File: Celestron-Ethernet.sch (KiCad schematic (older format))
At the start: 60 parts, among them J1 FTDI, J2 RJ45_Amphenol_RJMG1BD3B8K1ANR, J3 6P6C, SW1 SW_Push, SW2 SW_DIP_x02, U1 W5500, U2 ATmega328P-AU, U3 74AHC1G125, U4 NCV33375ST-3.3, Y1 8MHz, Y2 25MHz

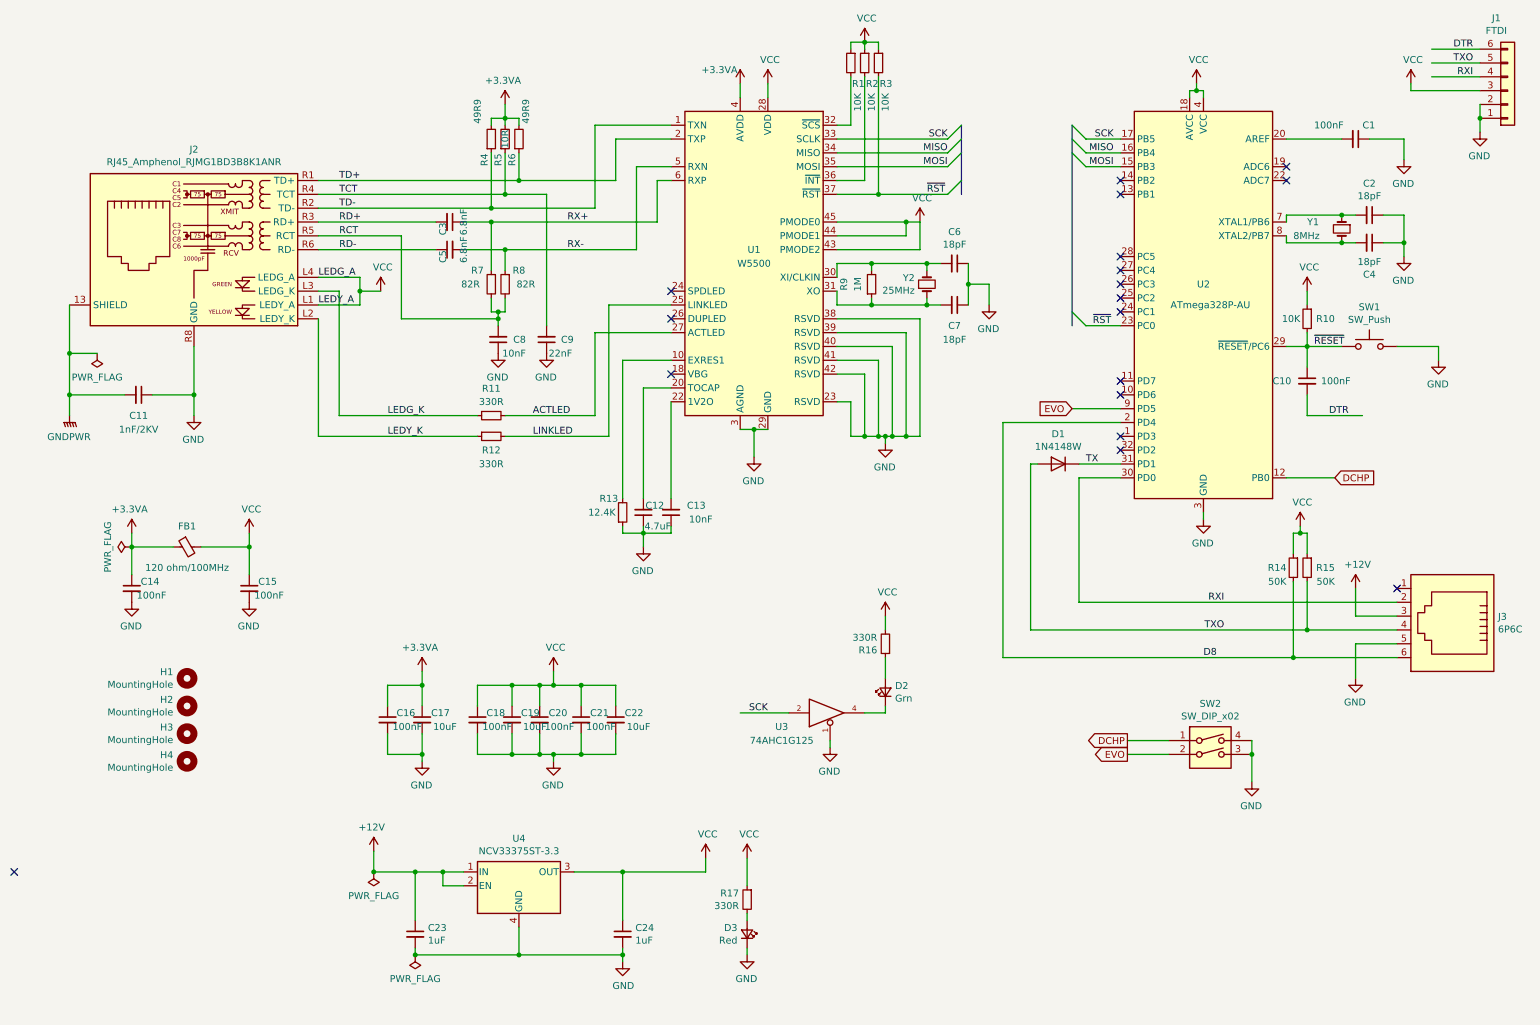
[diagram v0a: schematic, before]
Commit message: Added GPS connectors
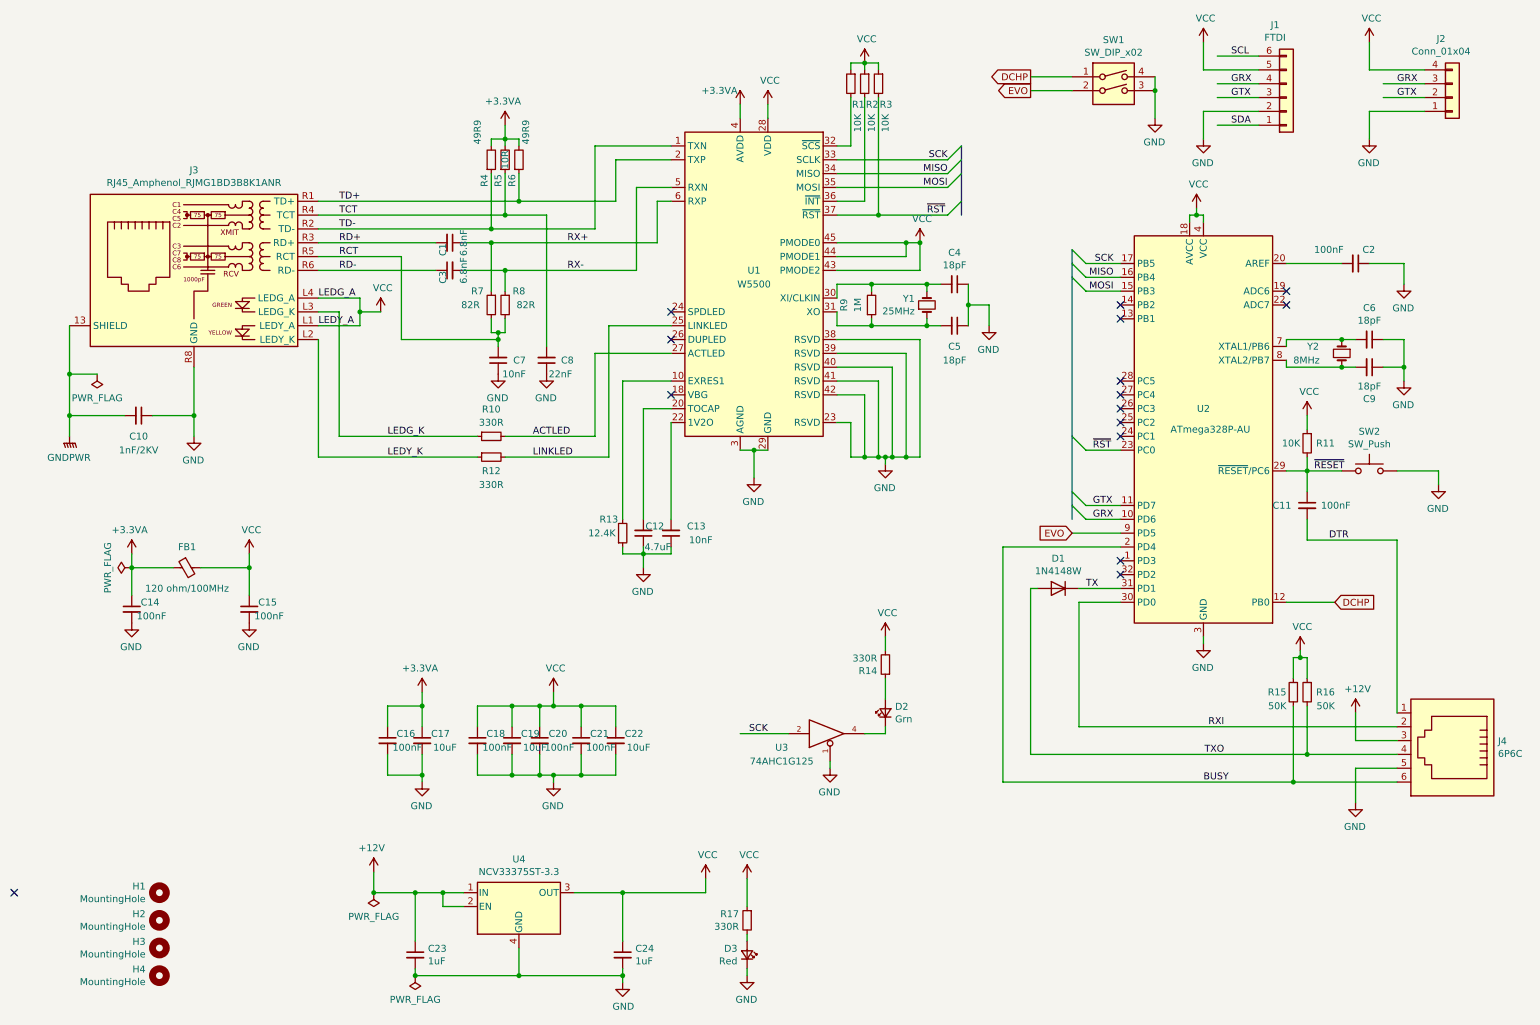
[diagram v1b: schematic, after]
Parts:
- added J2: Conn_01x04, Connector_JST:JST_SH_SM04B-SRSS-TB_1x04-1MP_P1.00mm_Horizontal, symbol Connector_Generic:Conn_01x04
- J1: footprint Connector_PinHeader_2.54mm:PinHeader_1x06_P2.54mm_Horizontal -> Connector_JST:JST_GH_SM06B-GHS-TB_1x06-1MP_P1.25mm_Horizontal
- renumbered C3 to C1, C11 to C10, C10 to C11, C1 to C2, C5 to C3, C6 to C4, C7 to C5, C2 to C6, C8 to C7, C9 to C8, C4 to C9, J2 to J3, J3 to J4, R11 to R10, R10 to R11, R16 to R14, R14 to R15, R15 to R16, SW2 to SW1, SW1 to SW2, Y2 to Y1, Y1 to Y2
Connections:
- net DTR: now also J4.1; no longer J1.6 (Pin_6)
- net GND: now also J2.1 (Pin_1); no longer J1.1 (Pin_1)
- net RXI: no longer J1.4 (Pin_4)
- net TXO: no longer J1.5 (Pin_5)
- net VCC: now also J1.5 (Pin_5), J2.4 (Pin_4); no longer J1.3 (Pin_3)
- net GRX: now reaches U2.10 (PD6)
- net GRX: now also J1.4 (Pin_4), J2.3 (Pin_3)
- net GTX: now reaches U2.11 (PD7)
- net GTX: now also J1.3 (Pin_3), J2.2 (Pin_2)
- net D8 renamed BUSY
- new net SCL: J1.6 (Pin_6)
- new net SDA: J1.1 (Pin_1)
- no-connect marks 18 -> 15
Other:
- moved on the sheet: C1, C10, C11, C12, C13, C14, C15, C16, C17, C18, C19, C2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

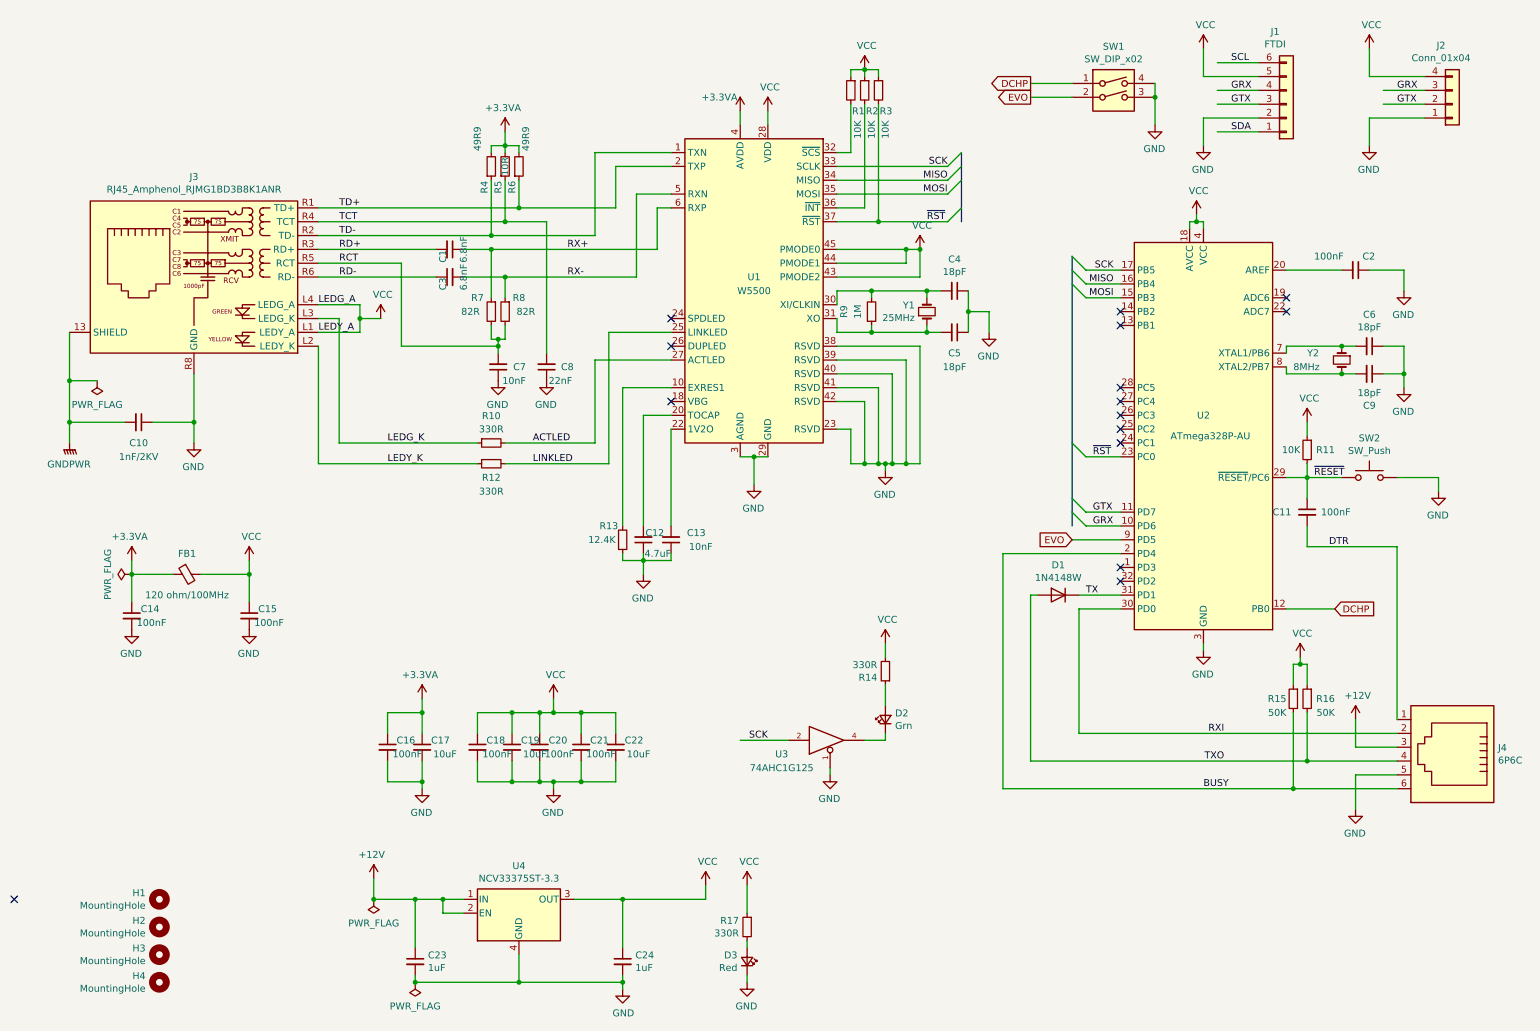
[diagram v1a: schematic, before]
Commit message: Separated W5500 schematic, added joystick interface
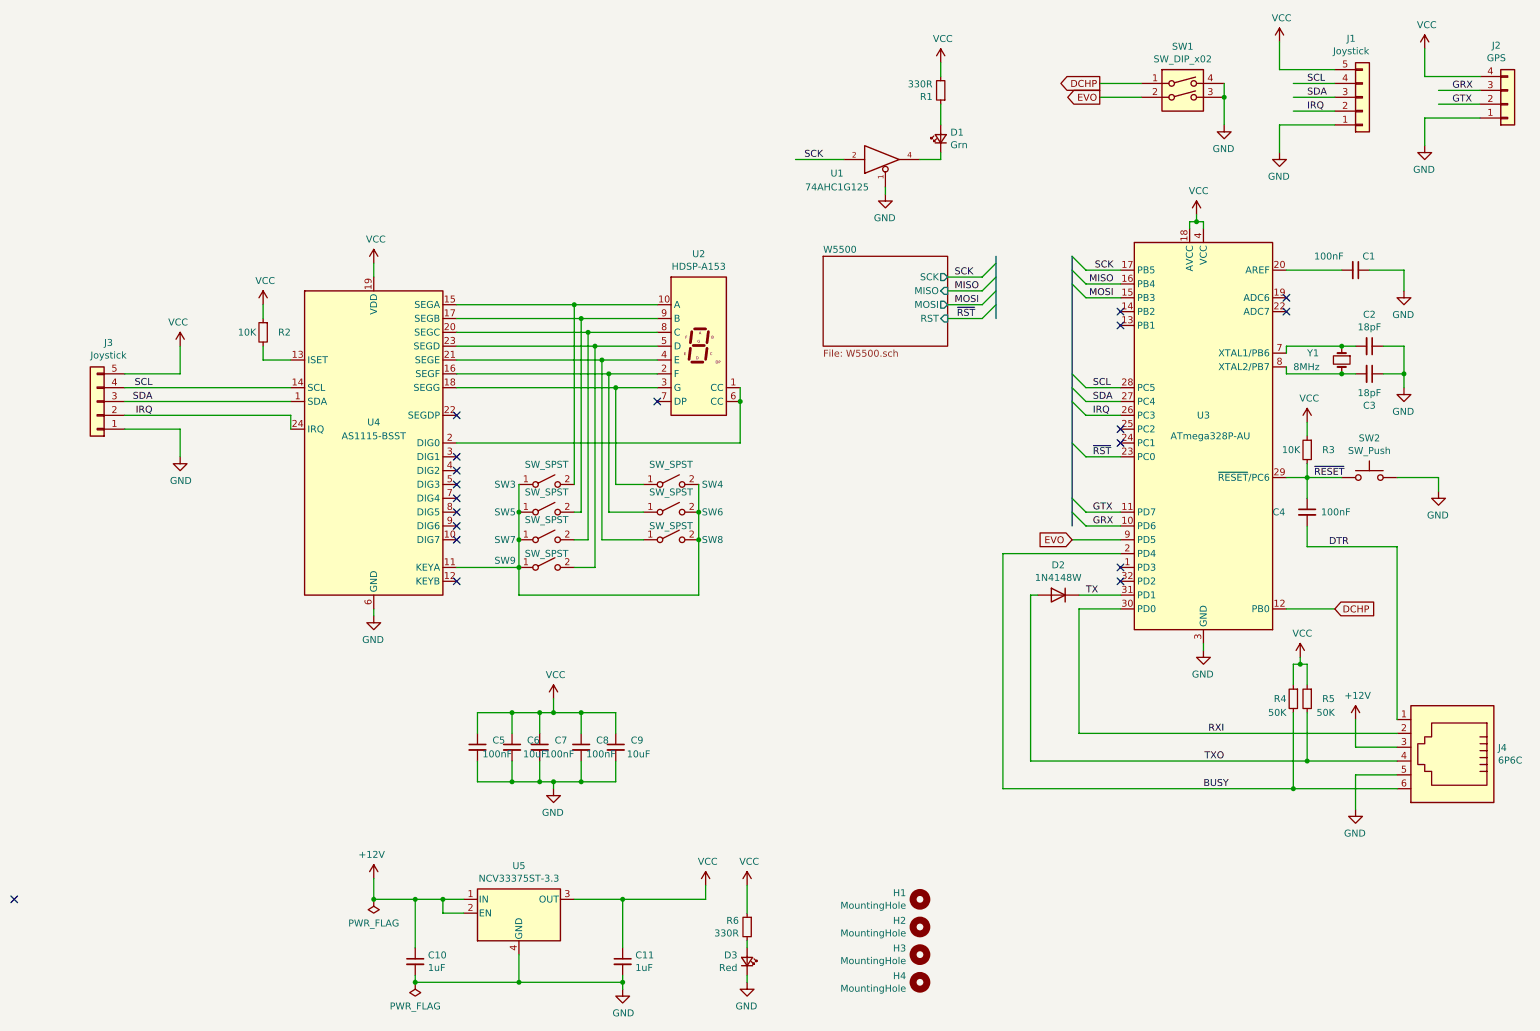
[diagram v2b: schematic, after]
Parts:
- removed C1, C3: 6.8nF, Capacitor_SMD:C_0603_1608Metric, symbol Device:C_Small
- removed C10: 1nF/2KV, Capacitor_SMD:C_1206_3216Metric, symbol Device:C_Small
- removed C12: 4.7uF, Capacitor_SMD:C_0603_1608Metric, symbol Device:C_Small
- removed C13, C7: 10nF, Capacitor_SMD:C_0603_1608Metric, symbol Device:C_Small
- removed C14, C15, C16: 100nF, Capacitor_SMD:C_0603_1608Metric, symbol Device:C_Small
- removed C17: 10uF, Capacitor_SMD:C_0603_1608Metric, symbol Device:C_Small
- removed C4, C5: 18pF, Capacitor_SMD:C_0603_1608Metric, symbol Device:C_Small
- removed C8: 22nF, Capacitor_SMD:C_0603_1608Metric, symbol Device:C_Small
- removed FB1: 120 ohm/100MHz, Inductor_SMD:L_0603_1608Metric, symbol Device:Ferrite_Bead_Small
- removed J1: FTDI, Connector_JST:JST_GH_SM06B-GHS-TB_1x06-1MP_P1.25mm_Horizontal, symbol Connector_Generic:Conn_01x06
- removed J3: RJ45_Amphenol_RJMG1BD3B8K1ANR, Connector_RJ:RJ45_Amphenol_RJMG1BD3B8K1ANR, symbol Connector:RJ45_Amphenol_RJMG1BD3B8K1ANR
- removed R1, R3: 10K, Resistor_SMD:R_0603_1608Metric, symbol Device:R_Small
- removed R10, R12: 330R, Resistor_SMD:R_0603_1608Metric, symbol Device:R_Small
- removed R13: 12.4K, Resistor_SMD:R_0603_1608Metric, symbol Device:R_Small
- removed R4, R6: 49R9, Resistor_SMD:R_0603_1608Metric, symbol Device:R_Small
- removed R5: 10R, Resistor_SMD:R_0603_1608Metric, symbol Device:R_Small
- removed R7, R8: 82R, Resistor_SMD:R_0603_1608Metric, symbol Device:R_Small
- removed R9: 1M, Resistor_SMD:R_0603_1608Metric, symbol Device:R_Small
- removed U1: W5500, Package_QFP:LQFP-48_7x7mm_P0.5mm, symbol Interface_Ethernet:W5500
- removed Y1: 25MHz, Crystal:Crystal_SMD_0603-2Pin_6.0x3.5mm, symbol Device:Crystal_Small
- added J1, J3: Joystick, Connector_JST:JST_SH_SM04B-SRSS-TB_1x05-1MP_P1.00mm_Horizontal, symbol Connector_Generic:Conn_01x05
- added SW3, SW4, SW5, SW6, SW7, SW8, SW9: SW_SPST, symbol Switch:SW_SPST
- added U2: HDSP-A153, Display_7Segment:HDSP-A151, symbol Display_Character:HDSP-A153
- added U4: AS1115-BSST, Package_SO:QSOP-24_3.9x8.7mm_P0.635mm, symbol Interface_Expansion:AS1115-BSST
- J2: value Conn_01x04 -> GPS
- renumbered C2 to C1, C23 to C10, C24 to C11, C6 to C2, C9 to C3, C11 to C4, C18 to C5, C19 to C6, C20 to C7, C21 to C8, C22 to C9, D2 to D1, D1 to D2, R14 to R1, R11 to R3, R15 to R4, R16 to R5, R17 to R6, U3 to U1, U2 to U3, U4 to U5, Y2 to Y1
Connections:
- net labels added: IRQ
- net labels removed: +3.3VA, ACTLED, GNDPWR, LEDG_A, LEDG_K, LEDY_A, LEDY_K, LINKLED, RCT, RD+, RD-, RX+, RX-, TCT, TD+, TD-
- wire segments 277 -> 184
- no-connect marks 15 -> 19
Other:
- moved on the sheet: D1, H1, H2, H3, H4, J2, R1, SW1, U1

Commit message: joystick interface
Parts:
- removed J3: Joystick, Connector_JST:JST_SH_SM04B-SRSS-TB_1x05-1MP_P1.00mm_Horizontal, symbol Connector_Generic:Conn_01x05
- removed R2: 10K, Resistor_SMD:R_0603_1608Metric, symbol Device:R_Small
- removed SW3, SW4, SW5, SW6, SW7, SW8, SW9: SW_SPST, symbol Switch:SW_SPST
- removed U2: HDSP-A153, Display_7Segment:HDSP-A151, symbol Display_Character:HDSP-A153
- removed U4: AS1115-BSST, Package_SO:QSOP-24_3.9x8.7mm_P0.635mm, symbol Interface_Expansion:AS1115-BSST
- added J?: Joystick, Connector_JST:JST_SH_SM04B-SRSS-TB_1x05-1MP_P1.00mm_Horizontal, symbol Connector_Generic:Conn_01x05
- added R?: 10K, Resistor_SMD:R_0603_1608Metric, symbol Device:R_Small
- added SW? (x7): SW_SPST, symbol Switch:SW_SPST
- added U?: HDSP-A153, Display_7Segment:HDSP-A151, symbol Display_Character:HDSP-A153
- added U?: AS1115-BSST, Package_SO:QSOP-24_3.9x8.7mm_P0.635mm, symbol Interface_Expansion:AS1115-BSST
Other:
- moved on the sheet: C10, C11, C5, C6, C7, C8, C9, D1, D3, J1, J2, R1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

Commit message: W5500 fixes
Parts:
- removed J?: Joystick, Connector_JST:JST_SH_SM04B-SRSS-TB_1x05-1MP_P1.00mm_Horizontal, symbol Connector_Generic:Conn_01x05
- removed R?: 10K, Resistor_SMD:R_0603_1608Metric, symbol Device:R_Small
- removed SW? (x7): SW_SPST, symbol Switch:SW_SPST
- removed U?: HDSP-A153, Display_7Segment:HDSP-A151, symbol Display_Character:HDSP-A153
- removed U?: AS1115-BSST, Package_SO:QSOP-24_3.9x8.7mm_P0.635mm, symbol Interface_Expansion:AS1115-BSST
- J1: footprint Connector_JST:JST_SH_SM04B-SRSS-TB_1x05-1MP_P1.00mm_Horizontal -> Connector_JST:JST_SH_BM05B-SRSS-TB_1x05-1MP_P1.00mm_Vertical
- J2: footprint Connector_JST:JST_SH_SM04B-SRSS-TB_1x04-1MP_P1.00mm_Horizontal -> Connector_JST:JST_SH_BM04B-SRSS-TB_1x04-1MP_P1.00mm_Vertical
- renumbered J4 to J3, R3 to R2, R4 to R3, R5 to R4, R6 to R5, U3 to U2, U5 to U3
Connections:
- wire segments 184 -> 132
- no-connect marks 19 -> 9
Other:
- moved on the sheet: C1, C2, C3, C4, C5, C6, C7, C8, C9, D1, D2, H1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

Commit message: cleanup
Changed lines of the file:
@@
 Wire Wire Line
 	5000 1600 5000 1400
-Text Label 5200 1700 0    50   ~ 0
+Text Label 5200 1900 0    50   ~ 0
 SCL
 Text Label 5200 1800 0    50   ~ 0
@@
 	5400 1800 5100 1800
 Wire Wire Line
-	5400 1700 5100 1700
+	5400 1900 5100 1900
 Wire Wire Line
 	5000 1600 5400 1600
@@
 	1    0    0    1
 $EndComp
-Text Label 5200 1900 0    50   ~ 0
+Text Label 5200 1700 0    50   ~ 0
 IRQ
 Wire Wire Line
-	5400 1900 5100 1900
+	5400 1700 5100 1700
 Entry Wire Line
 	7300 2200 7400 2300

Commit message: final version
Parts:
- removed C5: 100nF, Capacitor_SMD:C_0603_1608Metric, symbol Device:C_Small
- removed C6: 10uF, Capacitor_SMD:C_0603_1608Metric, symbol Device:C_Small
- added C7: 100nF, Capacitor_SMD:C_0603_1608Metric, symbol Device:C_Small
- C10: renamed from C11; value 1uF -> 100nF
- Y1: MPN 406C35D16M00000 -> 406C35D08M00000
- renumbered C7 to C5, C8 to C6, C10 to C8, R2 to R1, R1 to R2, U2 to U1, U1 to U2
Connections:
- wire segments 132 -> 126
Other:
- moved on the sheet: C10, C9, D3, R5

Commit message: buck converter
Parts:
- removed C8: 1uF, Capacitor_SMD:C_0603_1608Metric, symbol Device:C_Small
- removed C9: 10uF, Capacitor_SMD:C_0603_1608Metric, symbol Device:C_Small
- removed H1, H2, H3, H4: MountingHole, MountingHole:MountingHole_3.2mm_M3, symbol Mechanical:MountingHole
- removed SW1: SW_DIP_x02, Button_Switch_SMD:SW_DIP_SPSTx02_Slide_6.7x6.64mm_W8.61mm_P2.54mm_LowProfile, symbol Switch:SW_DIP_x02
- removed U3: NCV33375ST-3.3, Package_TO_SOT_SMD:SOT-223, symbol Regulator_Linear:NCV33375ST-3.3
- added C10: 68uF, Capacitor_Tantalum_SMD:CP_EIA-2012-12_Kemet-R, symbol Device:CP_Small
- added C9: 100uF, Capacitor_Tantalum_SMD:CP_EIA-2012-12_Kemet-R, symbol Device:CP_Small
- added D4: CDBUR0230, Diode_SMD:D_0603_1608Metric, symbol Device:D_Schottky
- added H1, H2, H3, H4: *, MountingHole:MountingHole_2.2mm_M2_Pad_Via, symbol Mechanical:MountingHole_Pad
- added JP1: DHCP, Connector_PinHeader_2.54mm:PinHeader_1x02_P2.54mm_Vertical, symbol Jumper:Jumper_2_Open
- added L1: 47uH, Inductor_SMD:L_Coilcraft_LPS5030, symbol Device:L_Small
- added U3: LM2672M-3.3, Package_SO:SOIC-8_3.9x4.9mm_P1.27mm, symbol Regulator_Switching:LM2672M-3.3
- C8: renamed from C10; value 100nF -> 10nF
- renumbered SW2 to SW1
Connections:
- net labels removed: DCHP, EVO
- wire segments 126 -> 127
- no-connect marks 9 -> 13
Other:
- moved on the sheet: C1, C2, C3, C4, C5, C6, C7, C8, D1, D2, D3, J1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
